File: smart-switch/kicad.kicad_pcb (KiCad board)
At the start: 2 copper layers, 54.1 x 27.7 mm, 15 parts, among them J1 KF350, J2 ESP8266, K1 JRC-21F(4100), Q1 MMBT4403

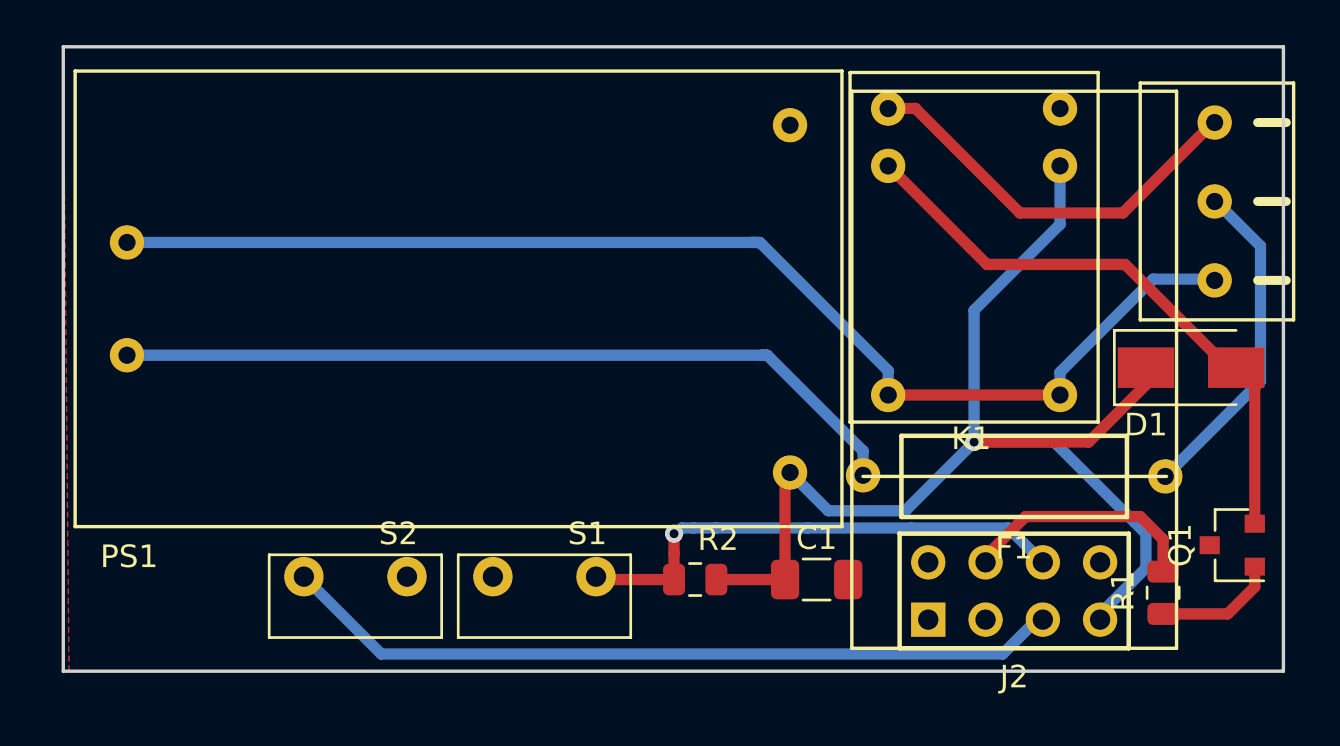
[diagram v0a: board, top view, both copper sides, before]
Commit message: Create esp01s-design project and 3d model for smart-switch
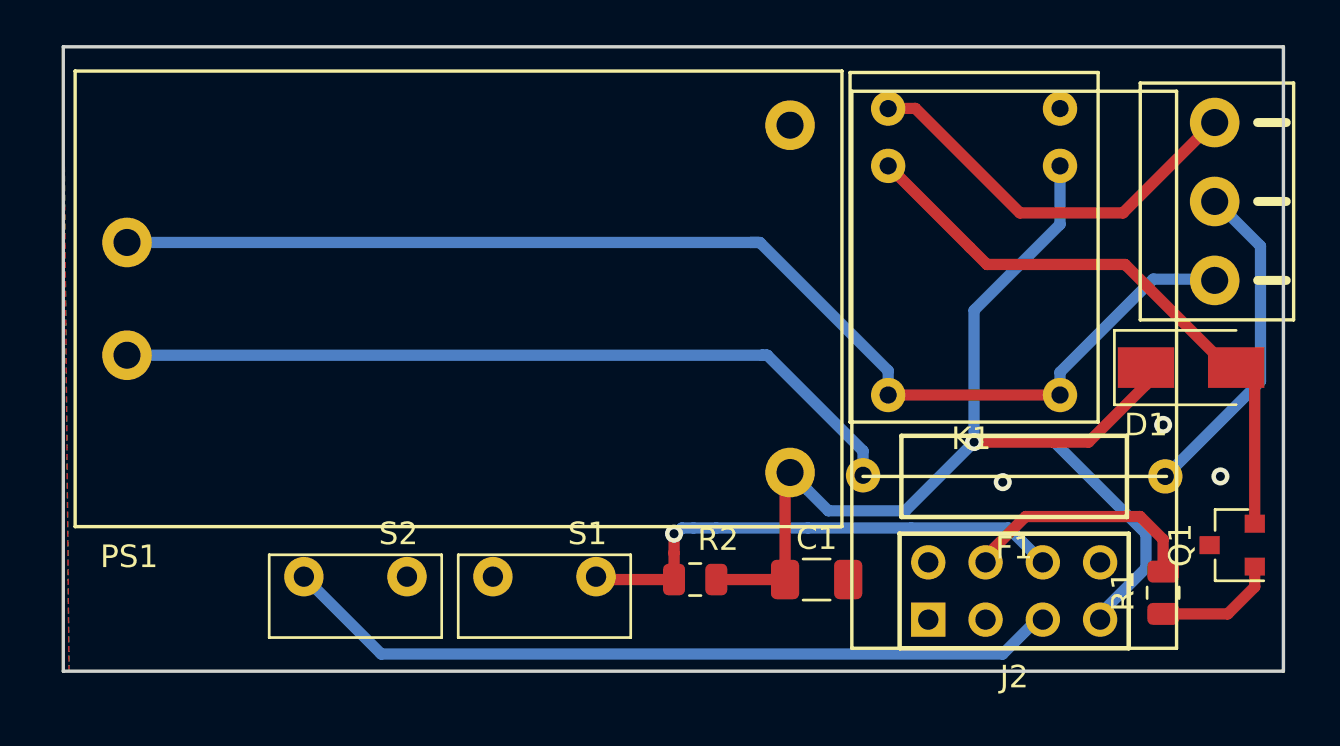
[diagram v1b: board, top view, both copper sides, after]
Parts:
- removed the G*** at (105.2, 90.4)
- removed the G*** at (102.9, 98.0)
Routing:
- net GND: vias 0 -> 3
- added copper zone on B.Cu, net GND
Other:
- net class Default removed

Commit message: Update smart switch 3d model
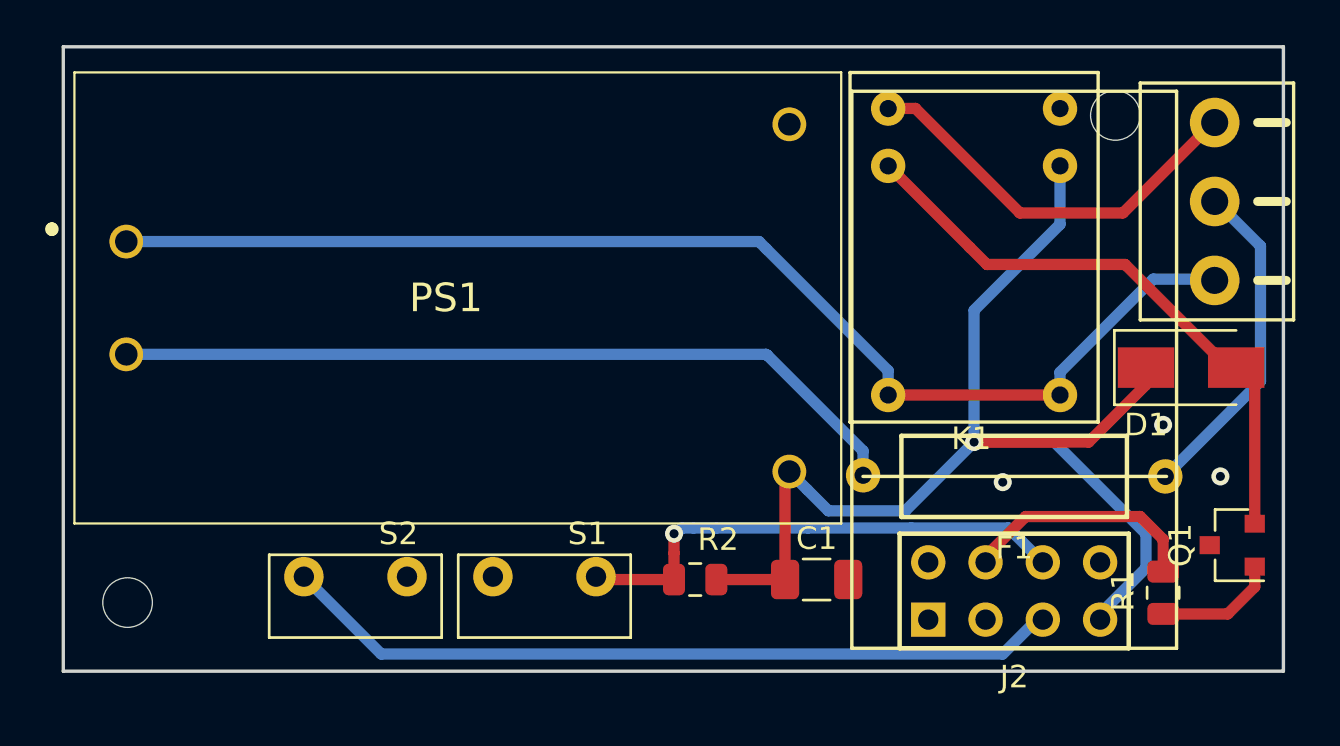
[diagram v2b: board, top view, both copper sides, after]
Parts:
- removed G***: LOGO, footprints:logo
- added REF**: Mounting_HOLES, footprints:Mounting_HOLES, F.Cu at (140.1, 75.3)
- PS1: value HLK-PM -> HLK-PM03; footprint footprints:HLK-PM -> HLK-PM03:HLKPM03
- R1: value 1K -> 10K
- R2: value 10K -> 1K
- S1: value init setup -> reset
- S2: value reset -> init setup
- moved PS1 14.9 mm to (115.8, 70.1)
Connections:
- J2 pad 1: Net-(J2-Pad1) -> unconnected-(J2-Pad1)
- J2 pad 2: Net-(J2-Pad2) -> unconnected-(J2-Pad2)
- J2 pad 5: Net-(J2-Pad5) -> unconnected-(J2-Pad5)
- K1 pad 3: Net-(K1-Pad3) -> unconnected-(K1-Pad3)
- R1 pad 1: Net-(Q1-Pad2) -> Net-(J2-Pad6)
- R1 pad 2: Net-(J2-Pad7) -> +3V3
- R2 pad 1: Net-(J2-Pad6) -> Net-(Q1-Pad2)
- R2 pad 2: +3V3 -> Net-(J2-Pad7)
- S1 pad 1: Net-(J2-Pad6) -> GND
- S1 pad 2: GND -> Net-(J2-Pad3)
- S2 pad 1: GND -> Net-(J2-Pad6)
- S2 pad 2: Net-(J2-Pad3) -> GND
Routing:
- net Net-(Q1-Pad2): track 5.46 -> 22.8 mm, vias 0 -> 1
- net Net-(J2-Pad6): track 22.8 -> 5.46 mm, vias 1 -> 0

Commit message: Update projects designs
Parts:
- added G***: LOGO, smart-home-schematic:logo, B.Cu at (133.0, 70.1)
- moved R1 20.8 mm to (141.0, 85.1), turned to 0 degrees
- moved R2 20.8 mm to (161.8, 85.6), turned to 90 degrees
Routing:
- net Net-(J2-Pad6): track 5.46 -> 32.3 mm, vias 0 -> 1
- net Net-(Q1-Pad2): track 22.8 -> 5.46 mm, vias 1 -> 0
- net Net-(J2-Pad3): track 34.9 -> 26.5 mm
- net Net-(F1-Pad2): track 14.8 -> 19.0 mm
- net Net-(F1-Pad1): track 35.5 -> 39.1 mm
- net +3V3: track 55.3 -> 54.5 mm
- net LINE: track 54.4 -> 55.1 mm
- net GND: track 0.00 -> 0.18 mm, vias 3 -> 2
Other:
- board text added: "V+"
- board text added: "V-"
